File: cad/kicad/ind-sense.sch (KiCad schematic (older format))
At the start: 29 parts, among them J1 Conn_01x27, J2 Conn_01x27, J3 Conn_01x18, U1 74HC154, U2 MCP4821, U5 CMP04, U6 CMP04

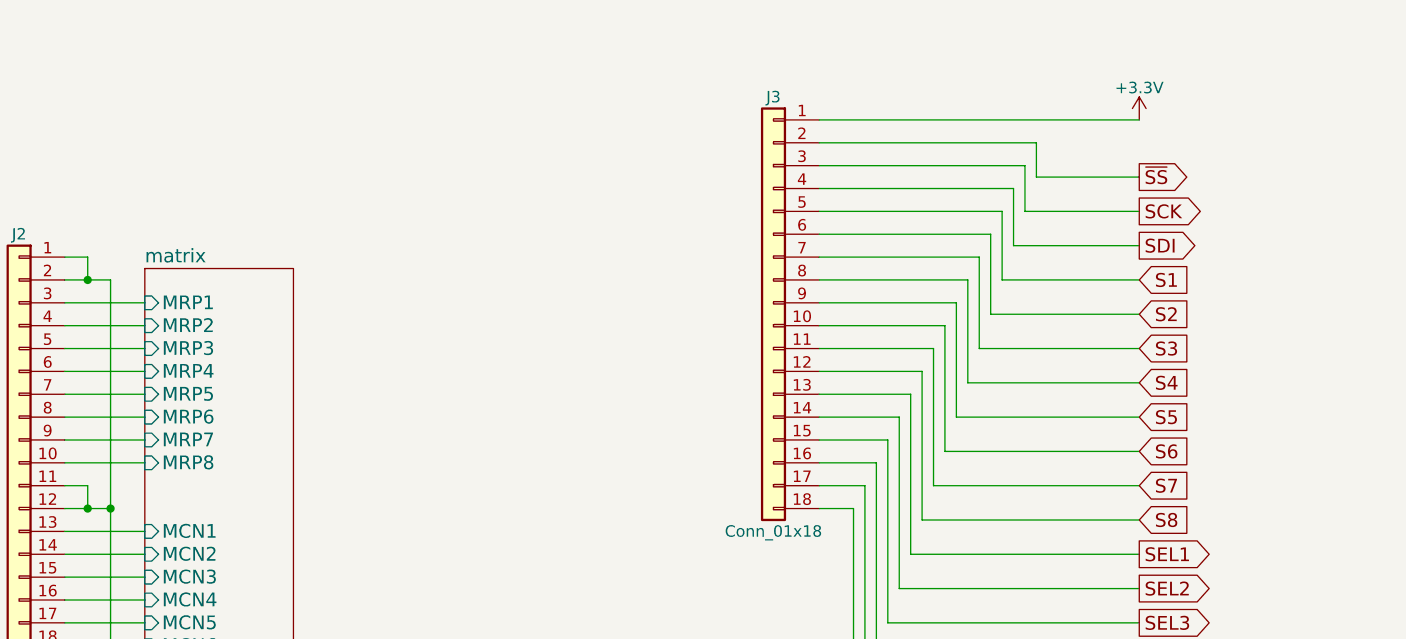
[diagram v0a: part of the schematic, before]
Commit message: updaded board and added some further documentation for egineering desicions, need to add further documentation to help people get up to speed with the project
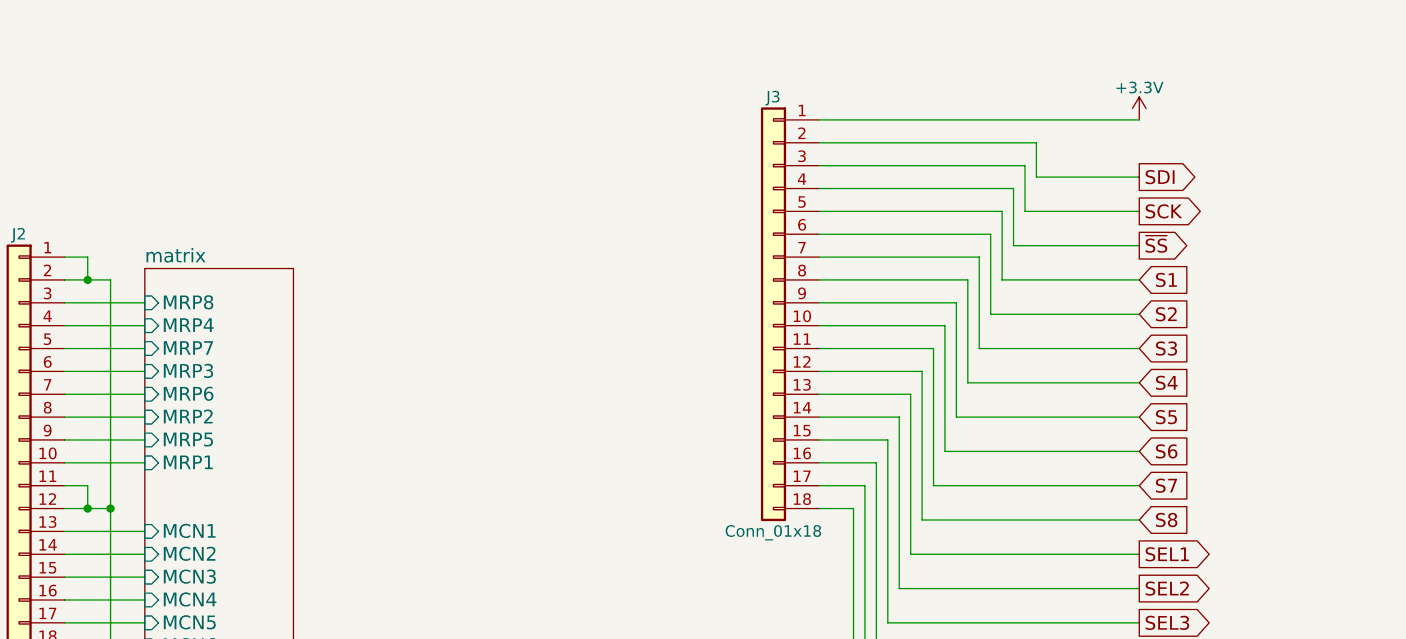
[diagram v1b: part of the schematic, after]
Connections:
- net SDI: now also J3.2 (Pin_2); no longer J3.4 (Pin_4)
- net matrix/MRP1: now also J2.10 (Pin_10); no longer J2.3 (Pin_3)
- net matrix/MRP2: now also J2.8 (Pin_8); no longer J2.4 (Pin_4)
- net matrix/MRP3: now also J2.6 (Pin_6); no longer J2.5 (Pin_5)
- net matrix/MRP4: now also J2.4 (Pin_4); no longer J2.6 (Pin_6)
- net matrix/MRP5: now also J2.9 (Pin_9); no longer J2.7 (Pin_7)
- net matrix/MRP6: now also J2.7 (Pin_7); no longer J2.8 (Pin_8)
- net matrix/MRP7: now also J2.5 (Pin_5); no longer J2.9 (Pin_9)
- net matrix/MRP8: now also J2.3 (Pin_3); no longer J2.10 (Pin_10)
- net ~SS: now also J3.4 (Pin_4); no longer J3.2 (Pin_2)
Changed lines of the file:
@@
 F12 "MCN11" I L 4600 9150 60
 F13 "MCN12" I L 4600 9250 60
-F14 "MRP1" I L 4600 7150 60
-F15 "MRP2" I L 4600 7250 60
-F16 "MRP3" I L 4600 7350 60
-F17 "MRP4" I L 4600 7450 60
-F18 "MRP5" I L 4600 7550 60
-F19 "MRP6" I L 4600 7650 60
-F20 "MRP7" I L 4600 7750 60
-F21 "MRP8" I L 4600 7850 60
+F14 "MRP1" I L 4600 7850 60
+F15 "MRP2" I L 4600 7650 60
+F16 "MRP3" I L 4600 7450 60
+F17 "MRP4" I L 4600 7250 60
+F18 "MRP5" I L 4600 7750 60
+F19 "MRP6" I L 4600 7550 60
+F20 "MRP7" I L 4600 7350 60
+F21 "MRP8" I L 4600 7150 60
 F22 "SHEILD" I L 4600 9550 60
 F23 "MCN13" I L 4600 9350 60
@@
 Text GLabel 8950 8850 2    60   Output ~ 0
 ~STROBE
-Text GLabel 8950 6600 2    60   Output ~ 0
+Text GLabel 8950 6900 2    60   Output ~ 0
 ~SS
 Text GLabel 8950 6750 2    60   Output ~ 0
 SCK
-Text GLabel 8950 6900 2    60   Output ~ 0
+Text GLabel 8950 6600 2    60   Output ~ 0
 SDI
 $Comp

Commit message: added logo, and started work on panelizing the demo pcb
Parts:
- removed C14, C15, C16, C17, C19, C20, C21, C22: 0u1, Capacitors_SMD:C_0603_HandSoldering, symbol C_Small
- added C5: 1u, Capacitors_SMD:C_0603_HandSoldering, symbol C_Small
- J1, J2: footprint Pin_Headers:Pin_Header_Straight_1x27_Pitch1.00mm -> Pin_Headers:Pin_Header_Straight_1x27_Pitch2.54mm
- J3: footprint Pin_Headers:Pin_Header_Straight_1x18_Pitch1.00mm -> Pin_Headers:Pin_Header_Straight_1x18_Pitch2.54mm
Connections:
- net GND: now also C5.2
- net M1: now also RN1.4 (R4.1), U5.10 (-); no longer RN1.1 (R1.1), U5.5 (+)
- net M2: now also RN1.3 (R3.1), U5.8 (-); no longer RN1.2 (R2.1), U5.7 (+)
- net M3: now also RN1.2 (R2.1), U5.4 (-); no longer RN1.3 (R3.1), U5.11 (+)
- net M4: now also RN1.1 (R1.1), U5.6 (-); no longer RN1.4 (R4.1), U5.9 (+)
- net M5: now also RN2.4 (R4.1), U6.10 (-); no longer RN2.1 (R1.1), U6.5 (+)
- net M6: now also RN2.3 (R3.1), U6.8 (-); no longer RN2.2 (R2.1), U6.7 (+)
- net M7: now also RN2.2 (R2.1), U6.4 (-); no longer RN2.3 (R3.1), U6.11 (+)
- net M8: now also RN2.1 (R1.1), U6.6 (-); no longer RN2.4 (R4.1), U6.9 (+)
- net S1: now also RN3.3 (R3.1), U5.13; no longer RN3.1 (R1.1), U5.2
- net S2: now also RN3.4 (R4.1), U5.14; no longer RN3.2 (R2.1), U5.1
- net S3: now also RN3.2 (R2.1), U5.2; no longer RN3.3 (R3.1), U5.13
- net S4: now also RN3.1 (R1.1), U5.1; no longer RN3.4 (R4.1), U5.14
- net S5: now also RN4.3 (R3.1), U6.13; no longer RN4.1 (R1.1), U6.2
- net S6: now also RN4.4 (R4.1), U6.14; no longer RN4.2 (R2.1), U6.1
- net S7: now also RN4.2 (R2.1), U6.2; no longer RN4.3 (R3.1), U6.13
- net S8: now also RN4.1 (R1.1), U6.1; no longer RN4.4 (R4.1), U6.14
- net SDI: now also J3.4 (Pin_4); no longer J3.2 (Pin_2)
- net SP: now also C4.1, U5.11 (+), U5.5 (+), U5.7 (+), U5.9 (+), U6.11 (+), U6.5 (+), U6.7 (+), U6.9 (+), C5.1; no longer U5.10 (-), U5.4 (-), U5.6 (-), U5.8 (-), U6.10 (-), U6.4 (-), U6.6 (-), U6.8 (-)
- net matrix/MRP2: now also J2.9 (Pin_9); no longer J2.8 (Pin_8)
- net matrix/MRP3: now also J2.8 (Pin_8); no longer J2.6 (Pin_6)
- net matrix/MRP4: now also J2.7 (Pin_7); no longer J2.4 (Pin_4)
- net matrix/MRP5: now also J2.6 (Pin_6); no longer J2.9 (Pin_9)
- net matrix/MRP6: now also J2.5 (Pin_5); no longer J2.7 (Pin_7)
- net matrix/MRP7: now also J2.4 (Pin_4); no longer J2.5 (Pin_5)
- net ~SS: now also J3.2 (Pin_2); no longer J3.4 (Pin_4)
- net at R4.1, U2.8 (Vout): no longer C4.1
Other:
- moved on the sheet: C4, R4, R5, R6
